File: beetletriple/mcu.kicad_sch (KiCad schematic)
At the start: 17 parts, among them J10 soicbite programming connector, J5 input_c1, J6 input_c2, J7 input_c3, J8 output_c4, J9 output_c5, U3 ATtiny1617-M

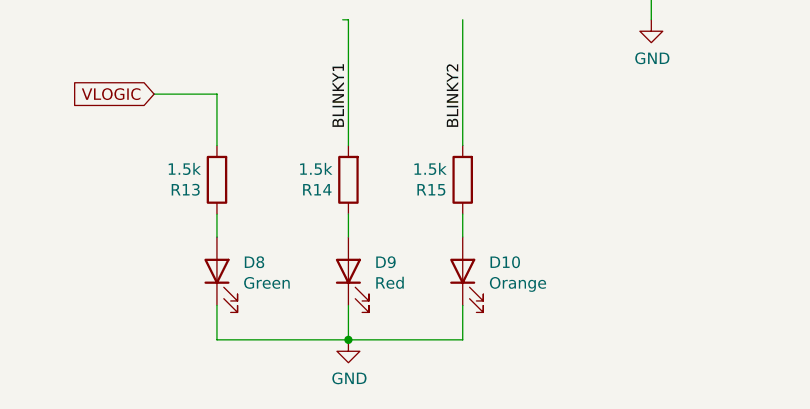
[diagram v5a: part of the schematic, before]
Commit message: add lcsc part numbers
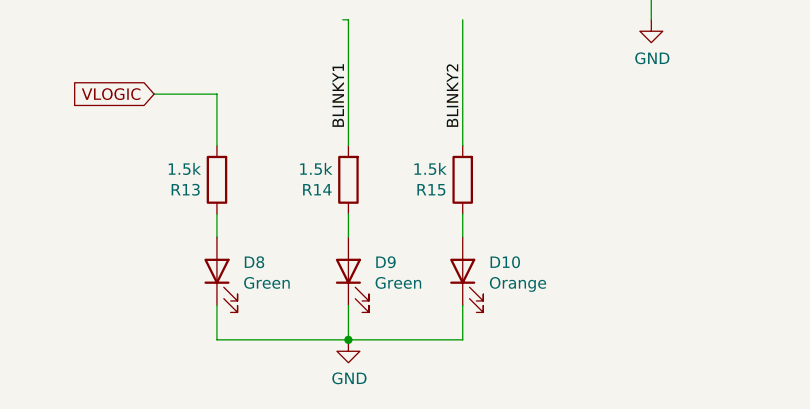
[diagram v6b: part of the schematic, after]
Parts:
- D10: LCSC (none) -> C84262
- D8: LCSC (none) -> C2297
- D9: value Red -> Green; LCSC (none) -> C2297
- R10, R11, R12, R13, R14, R15: LCSC (none) -> C4310
- U3: LCSC (none) -> C194193
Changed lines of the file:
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@@
+      (effects (font (size 1.27 1.27)) hide)
+    )
+    (property "LCSC" "C4310" (id 4) (at 40.005 104.775 0)
       (effects (font (size 1.27 1.27)) hide)
     )
@@
       (effects (font (size 1.27 1.27)) hide)
     )
+    (property "LCSC" "C4310" (id 4) (at 40.64 70.485 0)
+      (effects (font (size 1.27 1.27)) hide)
+    )
     (pin "1")
     (pin "2")
@@
       (effects (font (size 1.27 1.27)) hide)
     )
+    (property "LCSC" "C4310" (id 4) (at 40.64 86.36 0)
+      (effects (font (size 1.27 1.27)) hide)
+    )
     (pin "1")
     (pin "2")
@@
       (effects (font (size 1.27 1.27)) hide)
     )
+    (property "LCSC" "C4310" (id 4) (at 81.28 150.495 0)
+      (effects (font (size 1.27 1.27)) hide)
+    )
     (pin "1")
     (pin "2")
@@
       (effects (font (size 1.27 1.27)) hide)
     )
+    (property "LCSC" "C4310" (id 4) (at 95.885 150.495 0)
+      (effects (font (size 1.27 1.27)) hide)
+    )
     (pin "1")
     (pin "2")
@@
       (effects (font (size 1.27 1.27)) hide)
     )
+    (property "LCSC" "C4310" (id 4) (at 108.585 150.495 0)
+      (effects (font (size 1.27 1.27)) hide)
+    )
     (pin "1")
     (pin "2")
@@
       (effects (font (size 1.27 1.27)) hide)
     )
+    (property "LCSC" "C2297" (id 4) (at 81.28 160.655 0)
+      (effects (font (size 1.27 1.27)) hide)
+    )
     (pin "1")
     (pin "2")
@@
       (effects (font (size 1.27 1.27)) (justify right))
     )
-    (property "Value" "Red" (id 1) (at 98.806 161.995 90)
+    (property "Value" "Green" (id 1) (at 98.806 161.995 90)
       (effects (font (size 1.27 1.27)) (justify right))
     )
@@
       (effects (font (size 1.27 1.27)) hide)
     )
+    (property "LCSC" "C2297" (id 4) (at 95.885 160.655 0)
+      (effects (font (size 1.27 1.27)) hide)
+    )
     (pin "1")
     (pin "2")
@@
     )
     (property "Datasheet" "~" (id 3) (at 108.585 160.655 0)
+      (effects (font (size 1.27 1.27)) hide)
+    )
+    (property "LCSC" "C84262" (id 4) (at 108.585 160.655 0)
       (effects (font (size 1.27 1.27)) hide)
     )
@@
       (effects (font (size 1.27 1.27)) hide)
     )
+    (property "LCSC" "C194193" (id 4) (at 129.54 101.6 0)
+      (effects (font (size 1.27 1.27)) hide)
+    )
